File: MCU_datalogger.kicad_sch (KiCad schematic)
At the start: 1 part

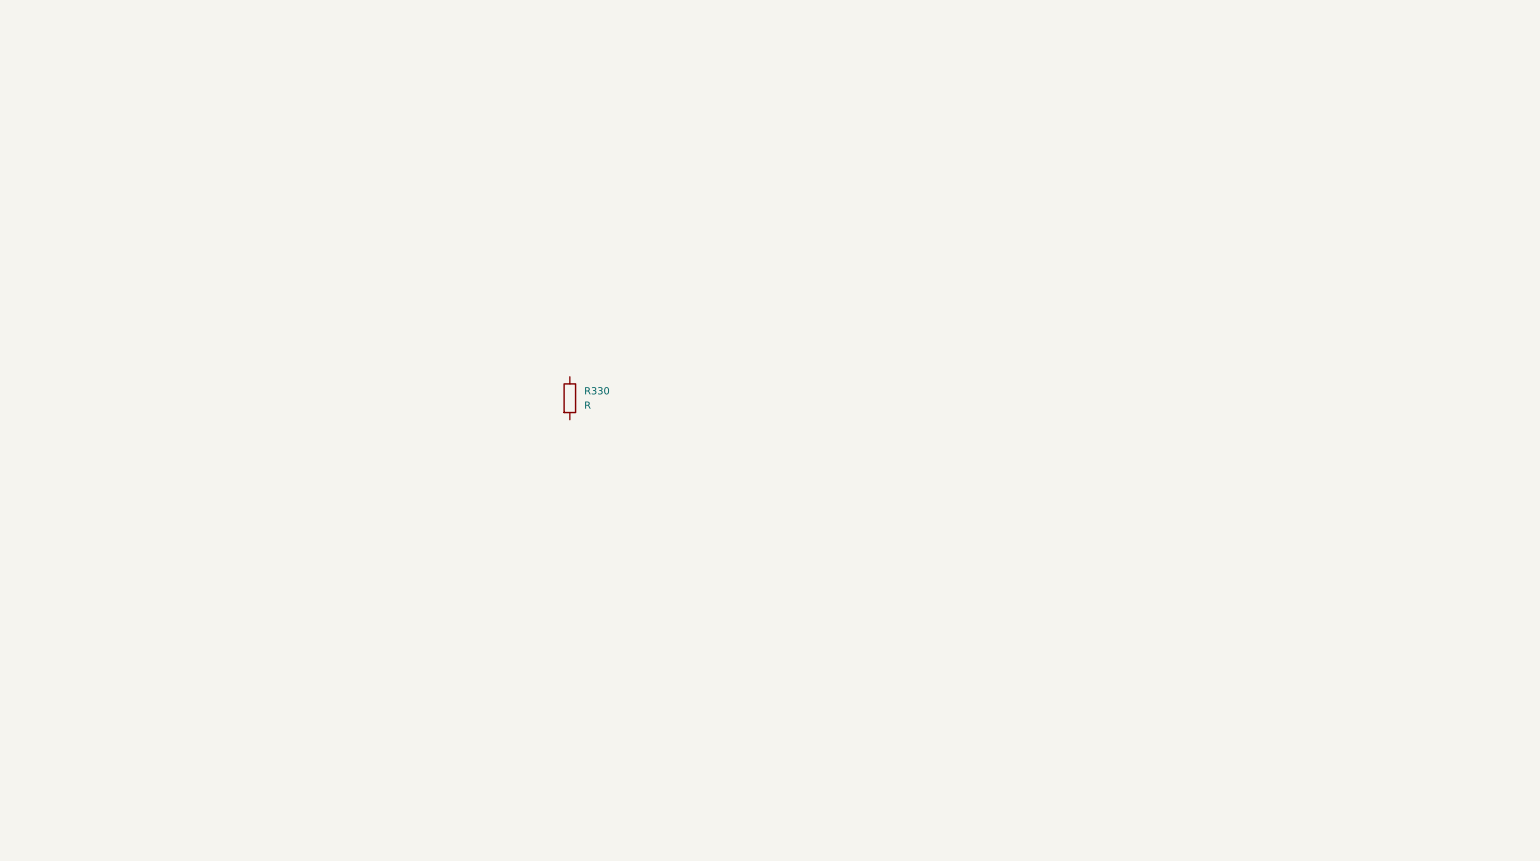
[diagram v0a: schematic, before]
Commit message: added all components to schema
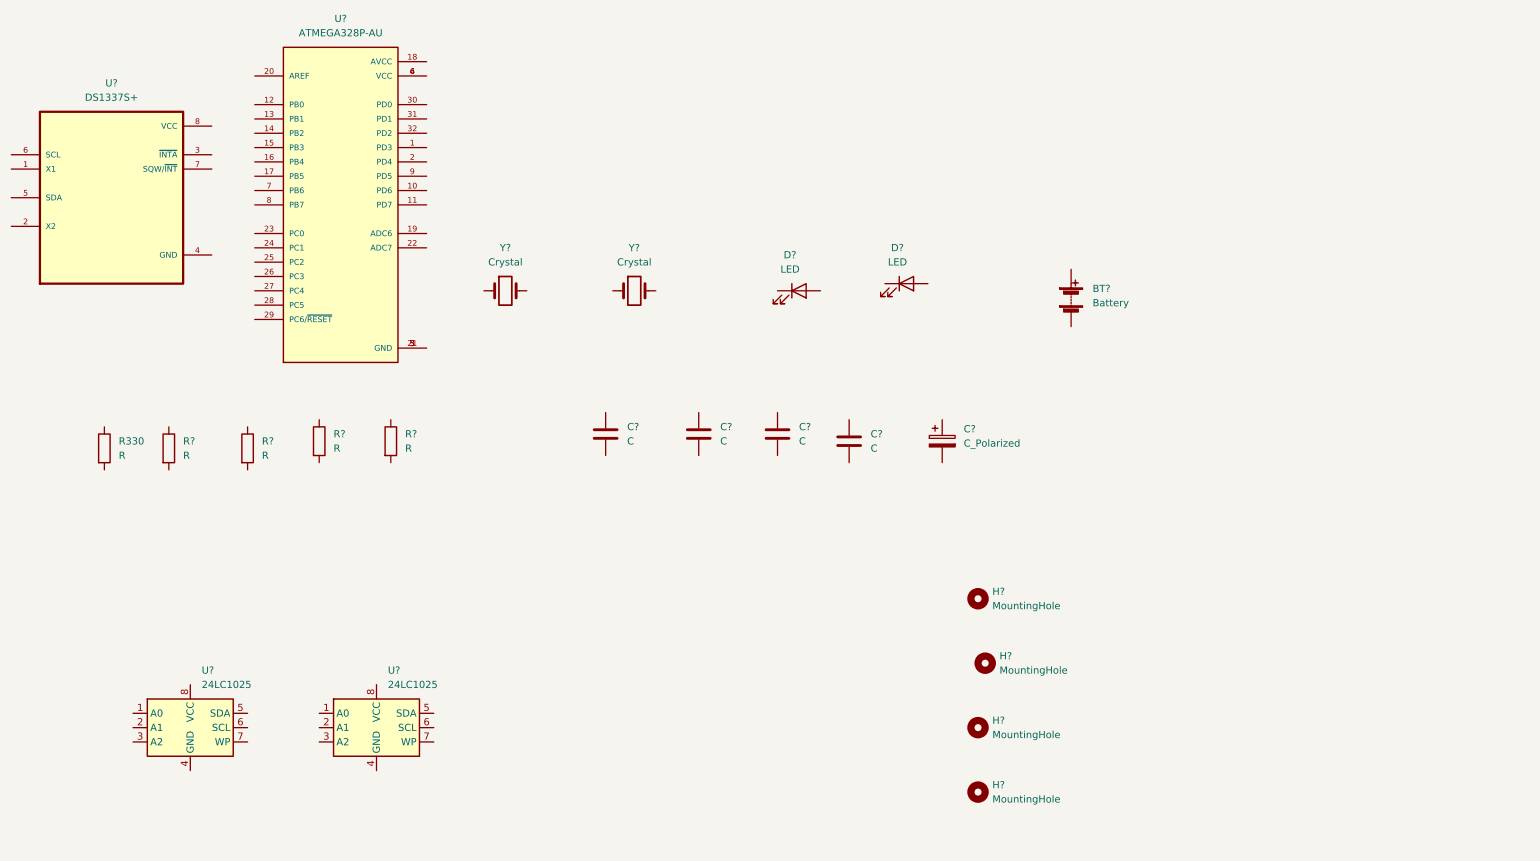
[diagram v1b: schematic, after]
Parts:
- added BT?: Battery, symbol Device:Battery
- added C? (x4): C, symbol Device:C
- added C?: C_Polarized, symbol Device:C_Polarized
- added D? (x2): LED, symbol Device:LED
- added H? (x4): MountingHole, symbol Mechanical:MountingHole
- added R? (x4): R, Resistor_THT:R_Axial_DIN0207_L6.3mm_D2.5mm_P10.16mm_Horizontal, symbol Device:R
- added U? (x2): 24LC1025, symbol Memory_EEPROM:24LC1025
- added U?: ATMEGA328P-AU, QFP80P900X900X120-32N, symbol ATMEGA328P-AU:ATMEGA328P-AU
- added U?: DS1337S+, SOIC127P600X175-8N, symbol DS1337S_:DS1337S+
- added Y? (x2): Crystal, symbol Device:Crystal
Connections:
- new net: U?.21 (GND), U?.3 (GND), U?.5 (GND)
- new net: U?.4 (VCC), U?.6 (VCC)
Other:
- title: (none) -> ${project_name}
- moved on the sheet: R330

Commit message: added symbol values
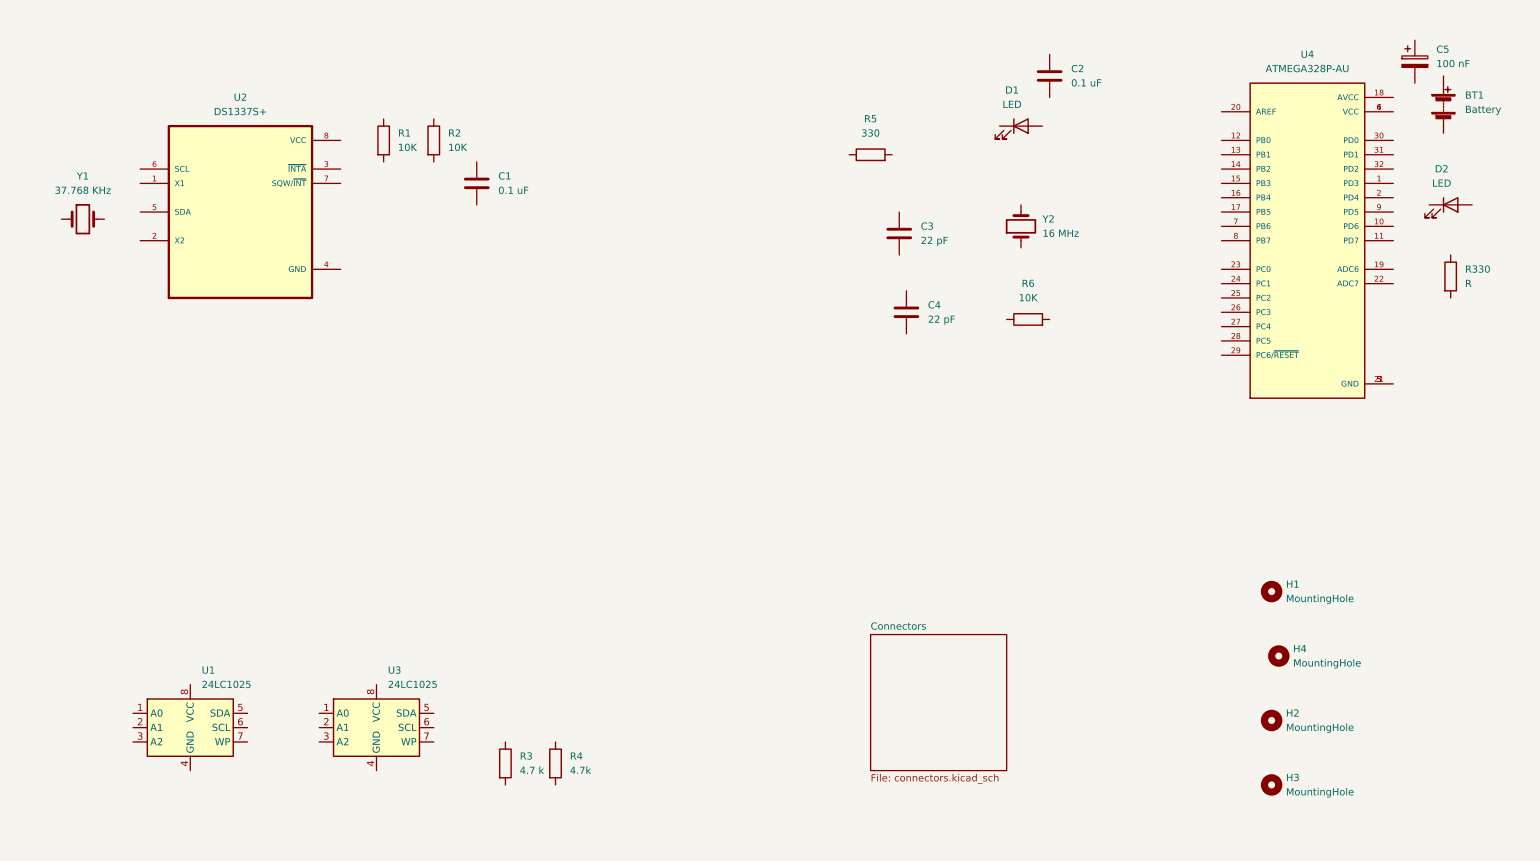
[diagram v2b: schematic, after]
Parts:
- added R4: 4.7k, Resistor_THT:R_Axial_DIN0207_L6.3mm_D2.5mm_P10.16mm_Horizontal, symbol Device:R
- added R6: 10K, Resistor_THT:R_Axial_DIN0207_L6.3mm_D2.5mm_P10.16mm_Horizontal, symbol Device:R
- C1, C2: renamed from C?; value C -> 0.1 uF
- C3, C4: renamed from C?; value C -> 22 pF
- C5: renamed from C?; value C_Polarized -> 100 nF
- R1, R2: renamed from R?; value R -> 10K
- R3: renamed from R?; value R -> 4.7 k
- R5: renamed from R?; value R -> 330
- Y1: renamed from Y?; value Crystal -> 37.768 KHz
- Y2: renamed from Y?; value Crystal -> 16 MHz
- gave numbers to parts that had none: 11
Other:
- added sheet Connectors (connectors.kicad_sch)
- moved on the sheet: BT1, C1, C2, C3, C4, C5, D1, D2, H1, H2, H3, H4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

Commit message: Completed the symbol foot prints
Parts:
- BT1: footprint (none) -> Connector_PinHeader_2.54mm:PinHeader_1x01_P2.54mm_Vertical
- C1, C2, C3, C4, C5: footprint (none) -> Capacitor_SMD:C_0805_2012Metric
- D1, D2: footprint (none) -> LED_SMD:LED_0805_2012Metric
- H1, H2, H3, H4: footprint (none) -> MountingHole:MountingHole_2.1mm
- R1, R2, R3, R330, R4, R5, R6: footprint Resistor_THT:R_Axial_DIN0207_L6.3mm_D2.5mm_P10.16mm_Horizontal -> Resistor_SMD:R_0805_2012Metric_Pad1.20x1.40mm_HandSolder
- U1, U3: footprint (none) -> Package_SO:SOIC-8_5.23x5.23mm_P1.27mm
- U2: footprint SOIC127P600X175-8N -> MCU_Footprints:SOIC127P600X175-8N
- U4: footprint QFP80P900X900X120-32N -> MCU_Footprints:QFP80P900X900X120-32N
- Y1, Y2: footprint (none) -> Crystal:Crystal_SMD_5032-2Pin_5.0x3.2mm

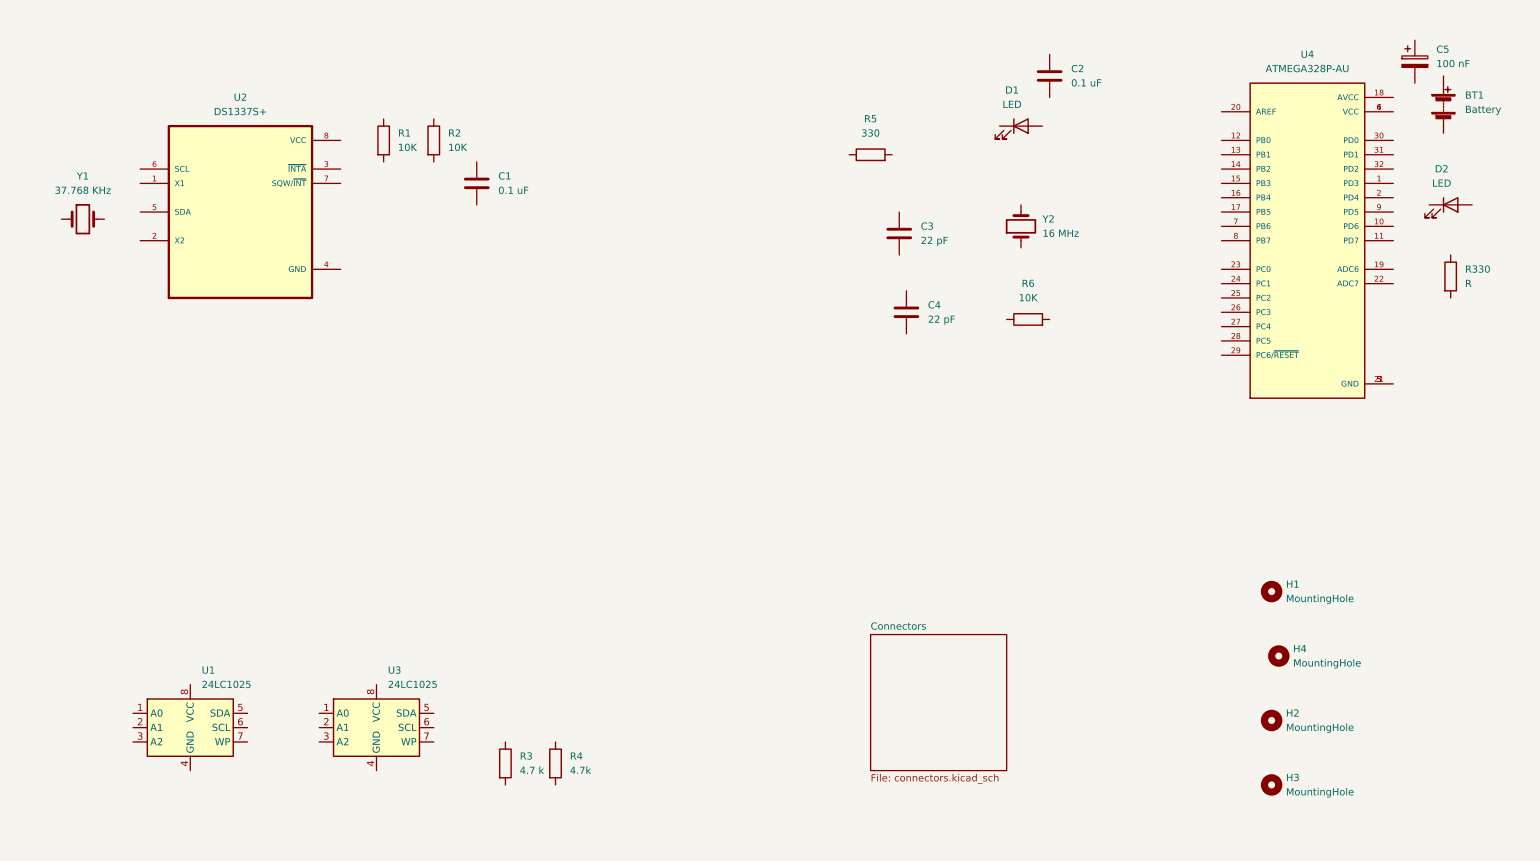
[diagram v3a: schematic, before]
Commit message: completed the wiring of main schema shteet
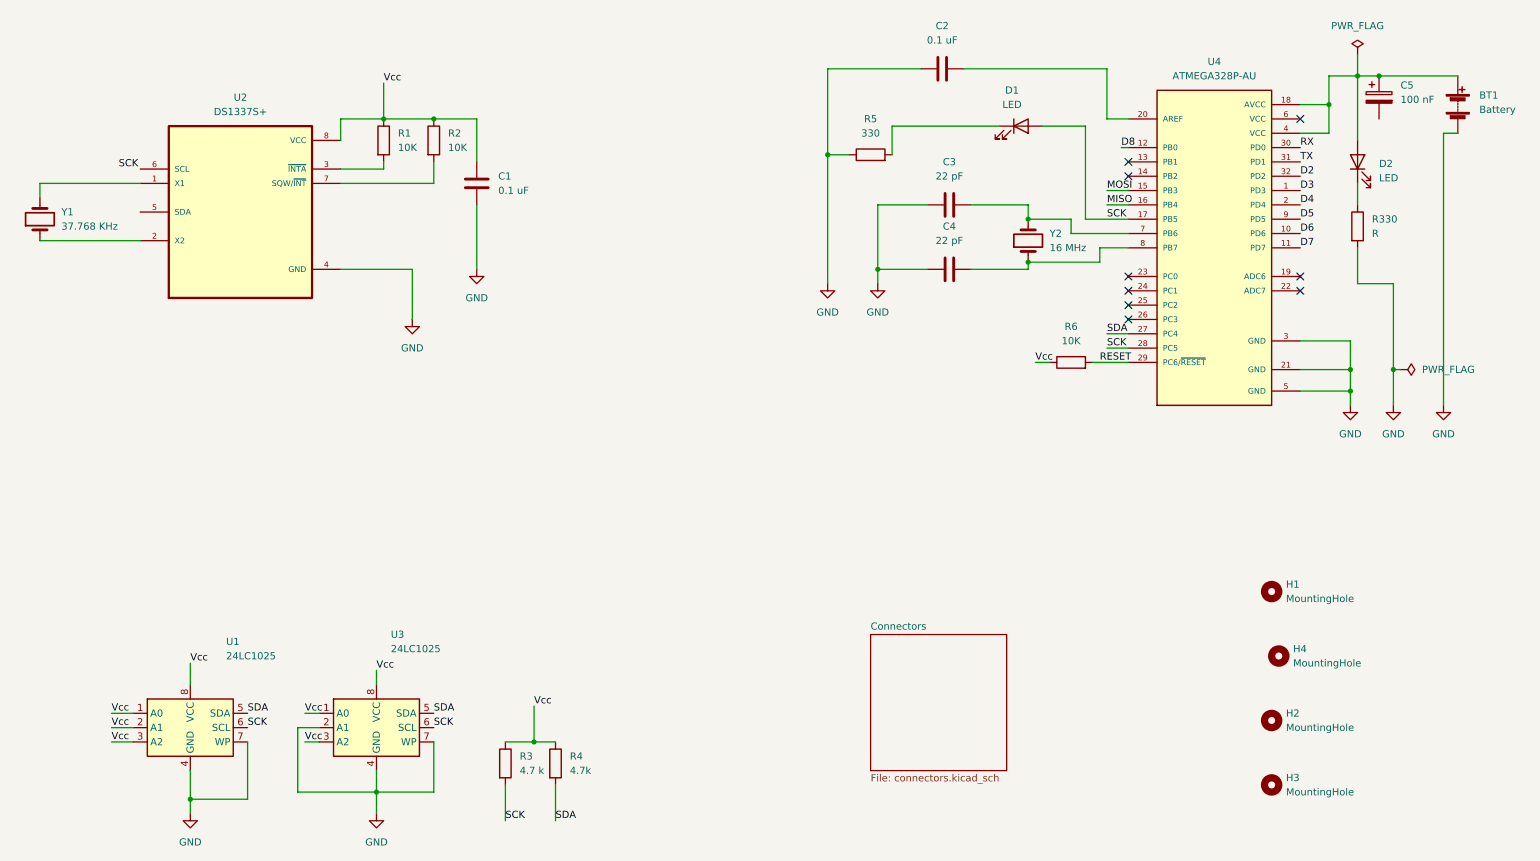
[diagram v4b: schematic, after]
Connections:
- net Vcc: now reaches R6.1
- net Vcc: now also C1.1, R1.1, R2.1, R3.1, R4.1, U1.1 (A0), U1.2 (A1), U1.3 (A2), U1.8 (VCC), U2.8 (VCC), U3.1 (A0), U3.3 (A2), U3.8 (VCC)
- net RESET: now reaches R6.2
- net RESET: now also U4.29 (PC6/~{RESET})
- net GND: now reaches U1.4 (GND)
- net GND: now also BT1.2 (-), C1.2, C2.1, C3.1, C4.1, R330.2, R5.1, U1.7 (WP), U2.4 (GND), U3.2 (A1), U3.4 (GND), U3.7 (WP), U4.21 (GND), U4.3 (GND), U4.5 (GND)
- net SDA: now reaches U1.5 (SDA)
- net SDA: now also R4.2, U3.5 (SDA), U4.27 (PC4)
- net SCK: now reaches U1.6 (SCL)
- net SCK: now also D1.2 (A), R3.2, U3.6 (SCL), U4.17 (PB5), U4.28 (PC5)
- net at D1.1 (K): now also R5.2
- net at C2.2: now also U4.20 (AREF)
- net at R330.1: now also D2.1 (K)
- net at R2.2: now also U2.7 (SQW/~{INT})
- net D3: now reaches U4.1 (PD3)
- net D6: now reaches U4.10 (PD6)
- net D7: now reaches U4.11 (PD7)
- net D8: now reaches U4.12 (PB0)
- net MOSI: now reaches U4.15 (PB3)
- net MISO: now reaches U4.16 (PB4)
- net at U4.18 (AVCC): now also BT1.1 (+), C5.1, D2.2 (A), U4.4 (VCC)
- net D4: now reaches U4.2 (PD4)
- net RX: now reaches U4.30 (PD0)
- net TX: now reaches U4.31 (PD1)
- net D2: now reaches U4.32 (PD2)
- net at U4.6 (VCC): no longer U4.4 (VCC)
- net at U4.7 (PB6): now also C3.2, Y2.2
- net at U4.8 (PB7): now also C4.2, Y2.1
- net D5: now reaches U4.9 (PD5)
- net at R1.2: now also U2.3 (~{INTA})
- net at Y1.1: now also U2.2 (X2)
- net at Y1.2: now also U2.1 (X1)
- no-connect marks 0 -> 9
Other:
- moved on the sheet: BT1, C2, C3, C4, C5, D2, R330, R6, Y1, Y2

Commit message: Finished wiring
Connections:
- net GND: now also C5.2
- net SCK: now also U2.6 (SCL)
- net SDA: now also U2.5 (SDA)
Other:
- sheet Connectors ports: added D2, D3, D4, D5, D6, D7, D8, GND, MISO, MOSI, RESET, RX, SCK, SDA, TX, Vcc; removed none
